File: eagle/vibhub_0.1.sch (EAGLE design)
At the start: 15 parts, among them U1 ESP-WROOM-32

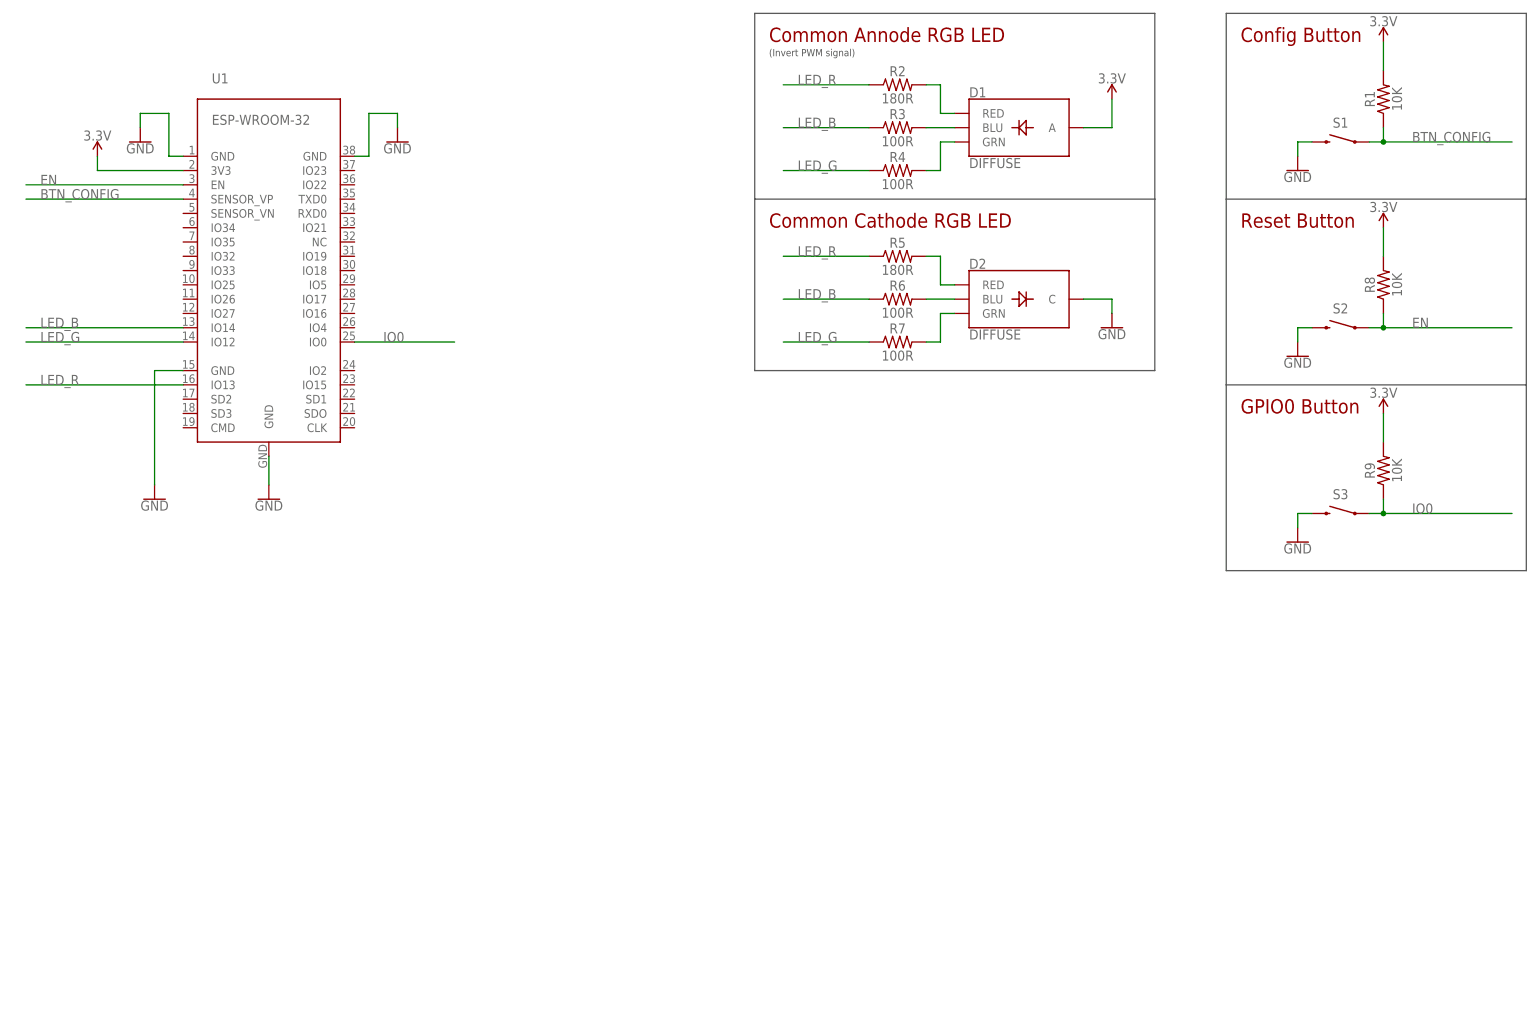
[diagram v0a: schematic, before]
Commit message: Added USB-to-UART interface
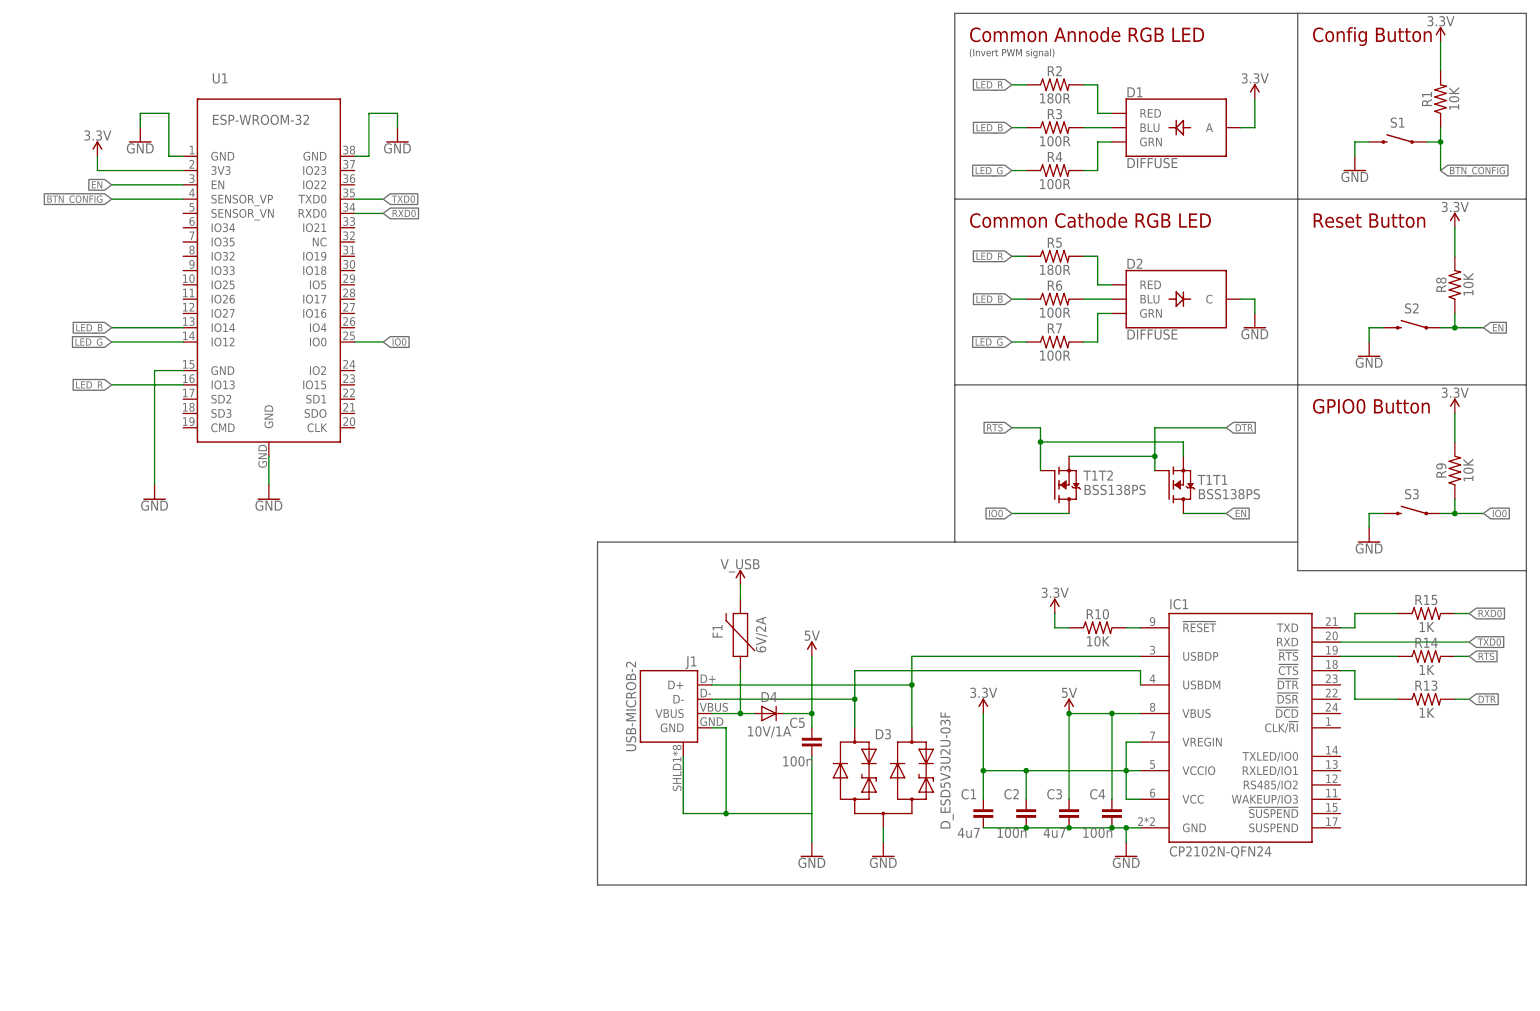
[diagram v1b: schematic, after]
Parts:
- added C1, C3: 4u7, vibhud:CAPACITOR-1206
- added C2, C4, C5: 100n, vibhud:CAPACITOR-1206
- added D3: D_ESD5V3U2U-03F, vibhud:D_ESD5V3U2U-03F
- added D4: 10V/1A, vibhud:DIODE-SMA
- added F1: 6V/2A, vibhud:PPTC_HALF-AMP
- added IC1: CP2102N-QFN24, vibhud:CP2102N-QFN24
- added J1: USB-MICROB-2, vibhud:USB-MICROB-2
- added R10: 10K, vibhud:RESISTOR0805
- added R13, R14, R15: 1K, vibhud:RESISTOR0805
- added T1: BSS138PS, vibhud:BSS138PS
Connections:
- new net 5V: C3.1, C4.1, C5.1, D4.C, IC1.VBUS
- new net DTR: R13.2, T1T1.G, T1T2.S
- new net N$10: IC1.!CTS, R13.1
- new net N$11: J1.GND, J1.SHIELD
- new net N$12: D4.A, F1.1, J1.VBUS
- new net N$7: IC1.!RESET, R10.2
- new net N$8: IC1.TXD, R15.1
- new net N$9: IC1.!RTS, R14.1
- new net RTS: R14.2, T1T1.S, T1T2.G
- new net RXD0: R15.2, U1.RXD0
- new net TXD0: IC1.RXD, U1.TXD0
- new net USB_DM: D3.C1, IC1.USBDM, J1.D-
- new net USB_DP: D3.C2, IC1.USBDP, J1.D+
- new net V_USB: F1.2
- net 3.3V: now also C1.1, C2.1, IC1.VCC, IC1.VCCIO, IC1.VREGIN, R10.1
- net EN: now also T1T1.D
- net GND: now also C1.2, C2.2, C3.2, C4.2, C5.2, D3.A, IC1.GND
- net IO0: now also T1T2.D
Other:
- moved on the sheet: D1, D2, R1, R2, R3, R4, R5, R6, R7, R8, R9, S1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

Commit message: Added input protection Added motor drivers Added motor outputs Added 12V DC input (motors only) Untested, will likely catch fire
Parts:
- added C10, C8: 0.1uF/16V, vibhud:CAPACITOR-1206
- added C11, C9: 10uF/16V, vibhud:CAPACITOR-0805
- added C12: 1.0uF, vibhud:CAPACITOR-1206
- added C13: 2.2uF, vibhud:CAPACITOR-1206
- added C6, C7: 0.1uF/6V, vibhud:CAPACITOR-0805
- added D5: 3A/40V/500mV, vibhud:DIODE-SCHOTTKY-B340A
- added J10: POWER_JACK, vibhud:POWER_JACK
- added J2, J3, J4, J5: USB-A-H, vibhud:USB-A-H
- added J6, J7, J8, J9: AUDIO_JACK_3.5MM_PTH, vibhud:AUDIO_JACK_3.5MM_PTH
- added Q1: 2.5A/30V/105mΩ, vibhud:MOSFET_PCH-DMG2307L
- added R11: 10K, vibhud:RESISTOR0805
- added R12: 1K, vibhud:RESISTOR0805
- added U2, U3: DRV8835, vibhud:DRV883X
- added U4: 3.3V, vibhud:V_REG_AP2112K-3.3V
- D4: value 10V/1A -> (none); device vibhud:DIODE-SMA -> vibhud:LED1206
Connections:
- removed net N$12: D4.A, F1.1, J1.VBUS
- new net 12V: D5.A, J10.PWR, Q1.G, R11.2
- new net MOTOR_0: U1.IO26, U2.AIN2/EN
- new net MOTOR_1: U1.IO25, U2.BIN2/EN
- new net MOTOR_2: U1.IO33, U3.AIN2/EN
- new net MOTOR_3: U1.IO32, U3.BIN2/EN
- new net MOT_0N: J2.GND, J6.RING, J6.RSH, U2.BOUT1
- new net MOT_0P: J2.VBUS, J6.TIP, J6.TSH, U2.AOUT1
- new net MOT_1N: J3.GND, J7.RING, J7.RSH, U2.BOUT2
- new net MOT_1P: J3.VBUS, J7.TIP, J7.TSH, U2.AOUT2
- new net MOT_2N: J4.GND, J8.RING, J8.RSH, U3.BOUT1
- new net MOT_2P: J4.VBUS, J8.TIP, J8.TSH, U3.AOUT1
- new net MOT_3N: J5.GND, J9.RING, J9.RSH, U3.BOUT2
- new net MOT_3P: J5.VBUS, J9.TIP, J9.TSH, U3.AOUT2
- new net VCC_1: C10.2, C11.2, C8.2, C9.2, D5.C, Q1.S, U2.VM, U3.VM
- net 3.3V: now also C13.1, C6.2, C7.2, R12.2, U2.MODE, U2.VCC, U3.MODE, U3.VCC, U4.OUT
- net 5V: now also C12.1, F1.2, Q1.D, U4.EN, U4.IN; no longer D4.C
- net GND: now also C10.1, C11.1, C12.2, C13.2, C6.1, C7.1, C8.1, C9.1, D4.C, J1.GND, J1.SHIELD, J10.GND, J10.GNDBREAK, J2.SHIELD, J3.SHIELD, J4.SHIELD, J5.SHIELD, J6.SLEEVE, J7.SLEEVE, J8.SLEEVE, J9.SLEEVE, R11.1, U2.AIN1/PH, U2.BIN1/PH, U2.VSS, U3.AIN1/PH, U3.BIN1/PH, U3.VSS, U4.GND
- net N$11: now also D4.A, R12.1; no longer J1.GND, J1.SHIELD
- net V_USB: now also F1.1, J1.VBUS; no longer F1.2
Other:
- note added: "Boot/Programming Control"
- note added: "Power/Data In/Protection"
- note added: "USB-to-UART"
- note added: "Wiring on 3.5mm jacks is likely very wrong here"

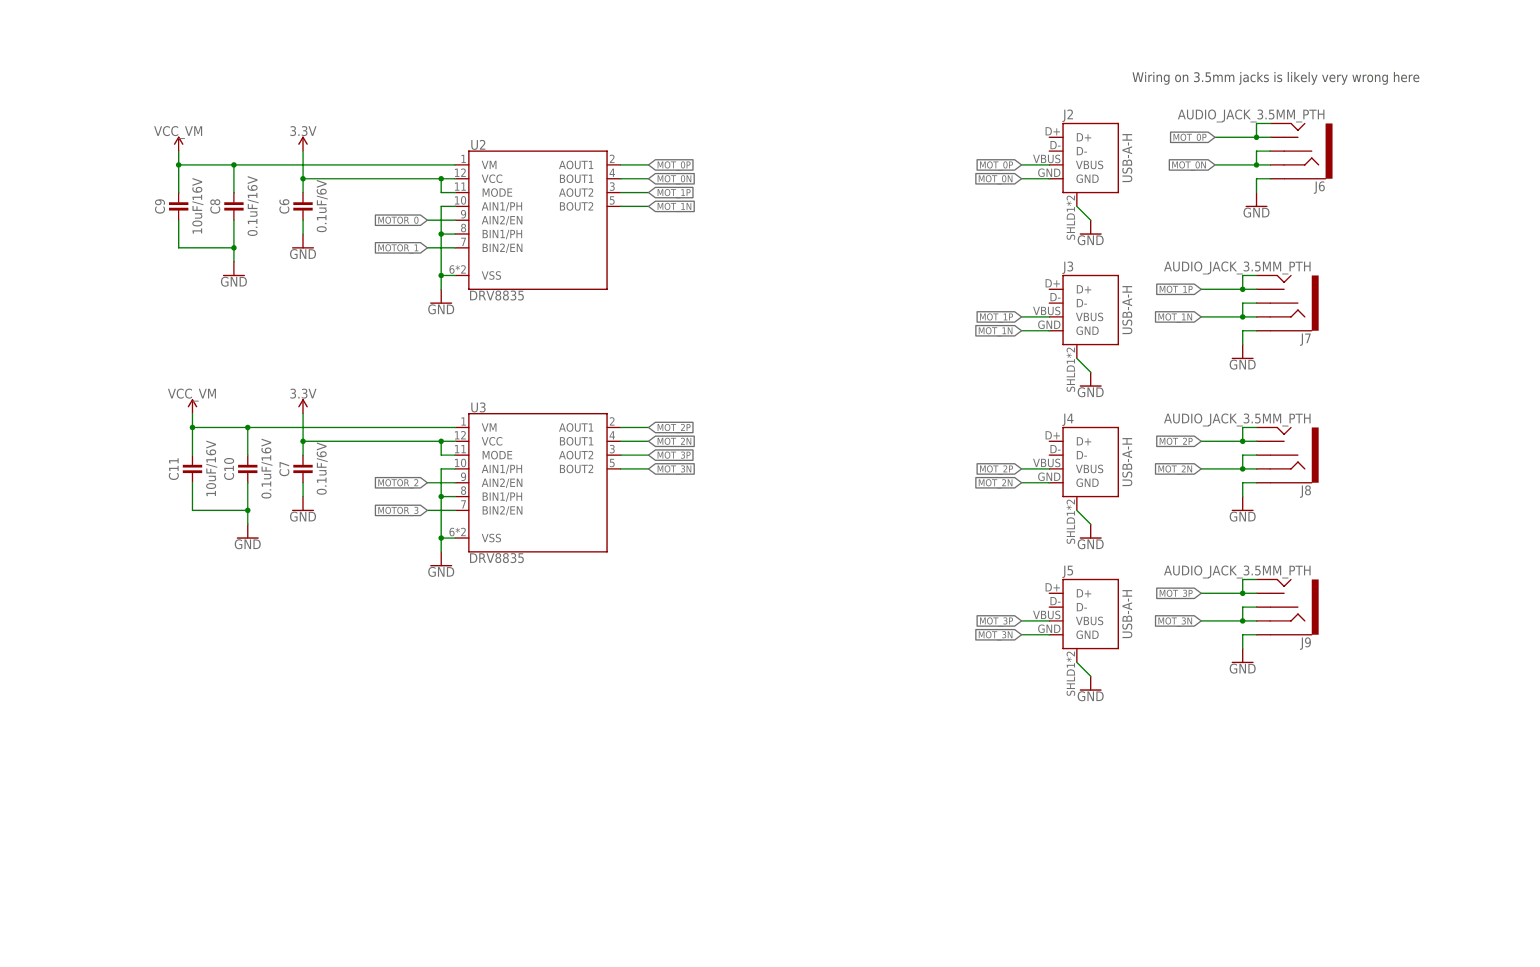
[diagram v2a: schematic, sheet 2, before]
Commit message: Added TB6612FNG driver option to schematic
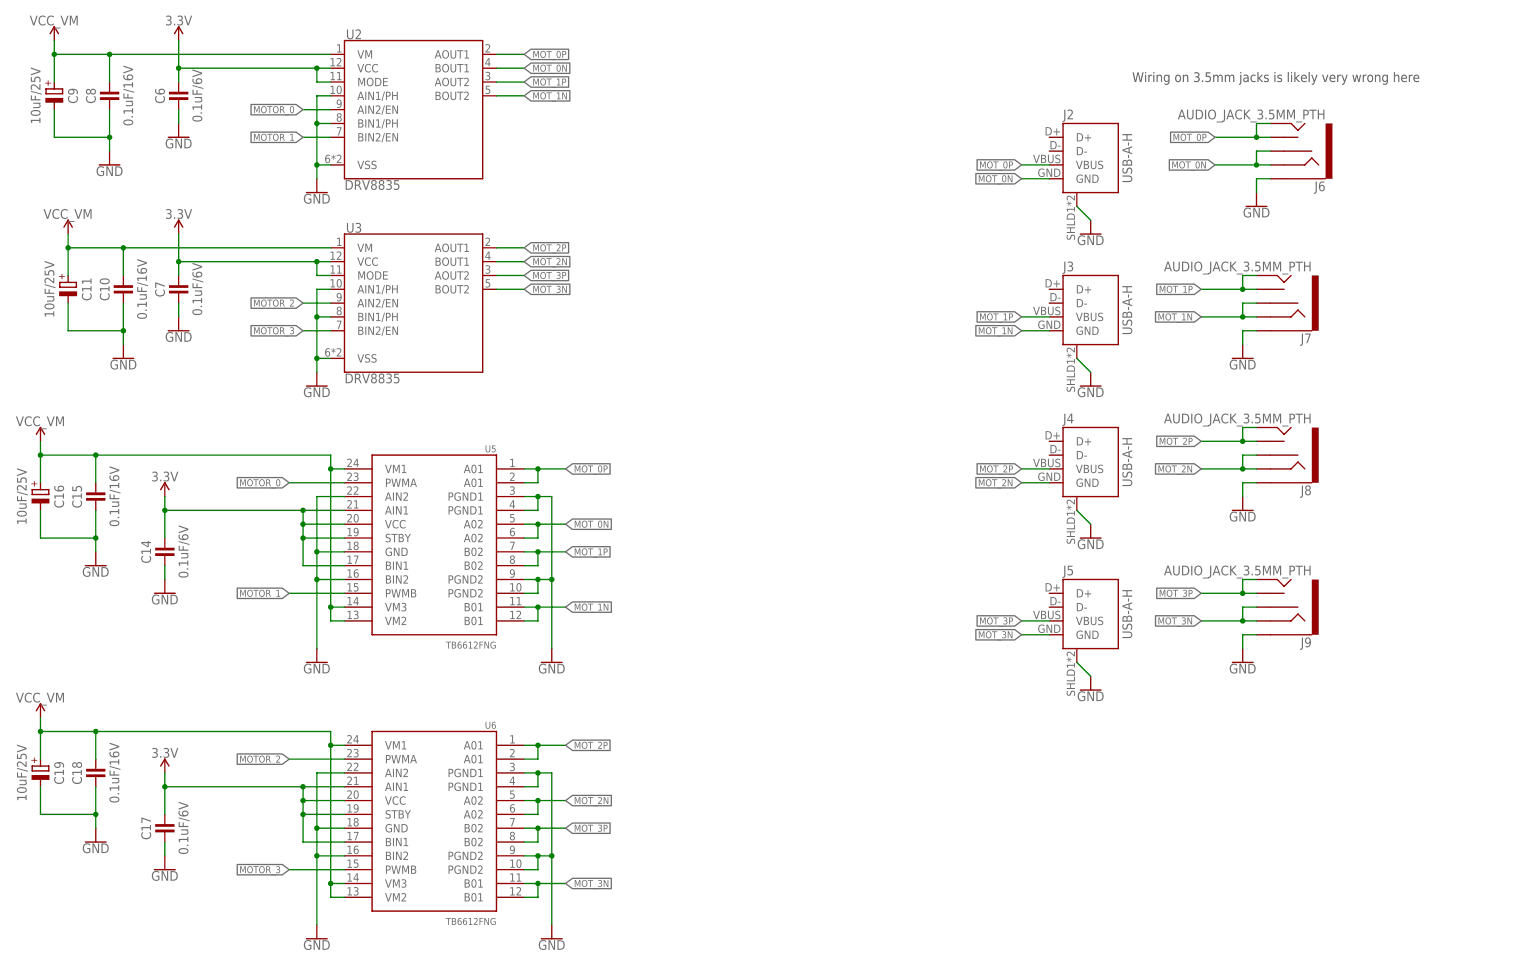
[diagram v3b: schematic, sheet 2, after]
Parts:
- added C14, C17: 0.1uF/6V, vibhud:CAPACITOR-0805
- added C15, C18: 0.1uF/16V, vibhud:CAPACITOR-1206
- added C16, C19: 10uF/25V, vibhud:CAPACITOR_POL-E2-4
- added U5, U6: TB6612FNG, vibhud:TB6612FNG
- C11, C9: value 10uF/16V -> 10uF/25V; device vibhud:CAPACITOR-0805 -> vibhud:CAPACITOR_POL-E2-4
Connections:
- net 3.3V: now also C14.2, C17.2, U5.AIN1, U5.BIN1, U5.STBY, U5.VCC, U6.AIN1, U6.BIN1, U6.STBY, U6.VCC
- net GND: now also C11.-, C14.1, C15.1, C16.-, C17.1, C18.1, C19.-, C9.-, U5.AIN2, U5.BIN2, U5.GND, U5.PGND1@3, U5.PGND1@4, U5.PGND2@10, U5.PGND2@9, U6.AIN2, U6.BIN2, U6.GND, U6.PGND1@3, U6.PGND1@4, U6.PGND2@10, U6.PGND2@9; no longer C11.1, C9.1
- net MOTOR_0: now also U5.PWMA
- net MOTOR_1: now also U5.PWMB
- net MOTOR_2: now also U6.PWMA
- net MOTOR_3: now also U6.PWMB
- net MOT_0N: now also U5.A02@5, U5.A02@6
- net MOT_0P: now also U5.A01@1, U5.A01@2
- net MOT_1N: now also U5.B01@11, U5.B01@12
- net MOT_1P: now also U5.B02@7, U5.B02@8
- net MOT_2N: now also U6.A02@5, U6.A02@6
- net MOT_2P: now also U6.A01@1, U6.A01@2
- net MOT_3N: now also U6.B01@11, U6.B01@12
- net MOT_3P: now also U6.B02@7, U6.B02@8
- net VCC_1: now also C11.+, C15.2, C16.+, C18.2, C19.+, C9.+, U5.VM1, U5.VM2, U5.VM3, U6.VM1, U6.VM2, U6.VM3; no longer C11.2, C9.2
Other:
- moved on the sheet: C10, C6, C7, C8, U2, U3

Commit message: Fleshed out the external power better This more likely will work now
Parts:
- removed R5: 180R, vibhud:RESISTOR0805
- removed R6, R7: 100R, vibhud:RESISTOR0805
- added C20: 470pF, vibhud:CAPACITOR-0805
- added C21: 2.2uF, vibhud:CAPACITOR-0805
- added JP2: JUMPER-SMT_3_NO_SILK, vibhud:JUMPER-SMT_3_NO_SILK
- added Q2: 1.1A/60V/600mΩ, vibhud:MOSFET_PCH-SI2309DS
- added U7: MIC5219 5V, vibhud:V_REG_MIC52195V
- C12, C13: device vibhud:CAPACITOR-1206 -> vibhud:CAPACITOR-0805
- D1: value DIFFUSE -> RGB; device vibhud:LED-RGB-CADIFFUSE -> vibhud:LED-RGB-CAPLCC
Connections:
- removed net N$2: D1.GRN, R4.2
- removed net N$6: D2.GRN, R7.2
- new net N$12: R3.2, U1.IO14
- new net N$13: R4.2, U1.IO12
- net 12V: now also Q2.G, U7.EN, U7.IN
- net 3.3V: now also JP2.1
- net 5V: now also C21.2, Q2.S, U7.OUT; no longer C5.1, F1.2, Q1.D
- net GND: now also C20.1, C21.1, JP2.3, U7.GND; no longer D2.C
- net LED_B: now also D1.BLU, D2.BLU; no longer R6.1, U1.IO14
- net LED_G: now also D1.GRN, D2.GRN; no longer R7.1, U1.IO12
- net LED_R: now also D1.RED, D2.RED; no longer R5.1, U1.IO13
- net N$1: now also D2.C, JP2.2; no longer D1.RED, R2.2
- net N$3: now also R2.2, U1.IO13; no longer D1.BLU, R3.2
- net N$4: now also C20.2, U7.BP; no longer D2.BLU, R6.2
- net N$5: now also F1.1, J1.VBUS; no longer D2.RED, R5.2
- net V_USB: now also C5.1, F1.2, Q1.D, Q2.D; no longer F1.1, J1.VBUS
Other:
- note added: "(Invert LED PWM output)"
- note added: "Common Annode SMD RGB LED"
- note added: "Ext 12V Input"
- note added: "TH RGB LED"
- note added: "USB Input"
- note removed: "(Invert PWM signal)"
- note removed: "Common Annode RGB LED"
- note removed: "Common Cathode RGB LED"
- note removed: "Power/Data In/Protection"
- moved on the sheet: C1, C12, C13, C2, C3, C4, C5, D1, D2, D3, D4, D5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
